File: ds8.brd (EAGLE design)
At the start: 127 x 66 mm, 114 parts, among them IC1 TM4C1230C3PM, IC2 TPS77333, IC3 DAC7512, J1 9VDC POSITIVE CENTER, Q1 BC850, Q2 BC850, Q3 BC850, U1 LM13700M, U100 VREG-7805-DPAK2, U2 LM324, U3 LM324, U4 LM741D, X1 MIDI IN, X2 MIDI OUT

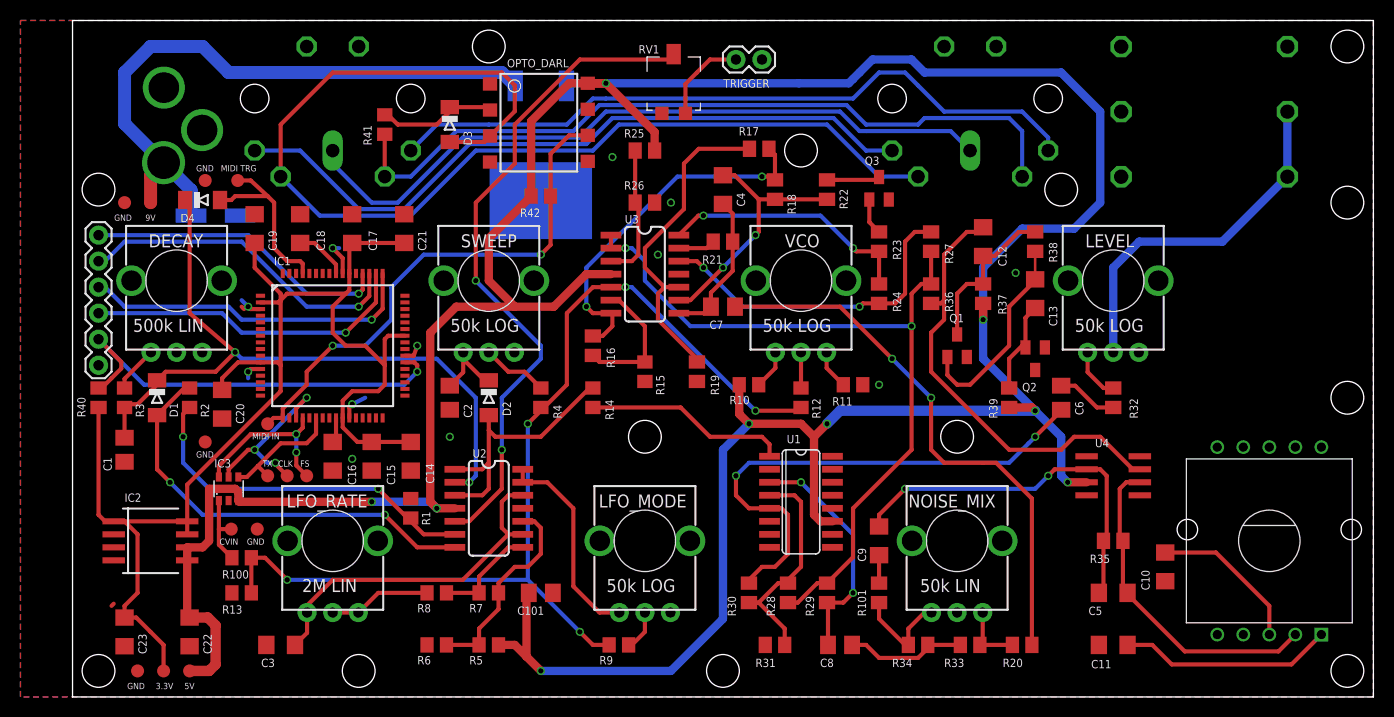
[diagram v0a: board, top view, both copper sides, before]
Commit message: Prototype v1
Version that has been produced via Seeed Studio.
Added todolist to readme.md.

Signed-off-by: Kamel Makhloufi <melka@blaste.net>
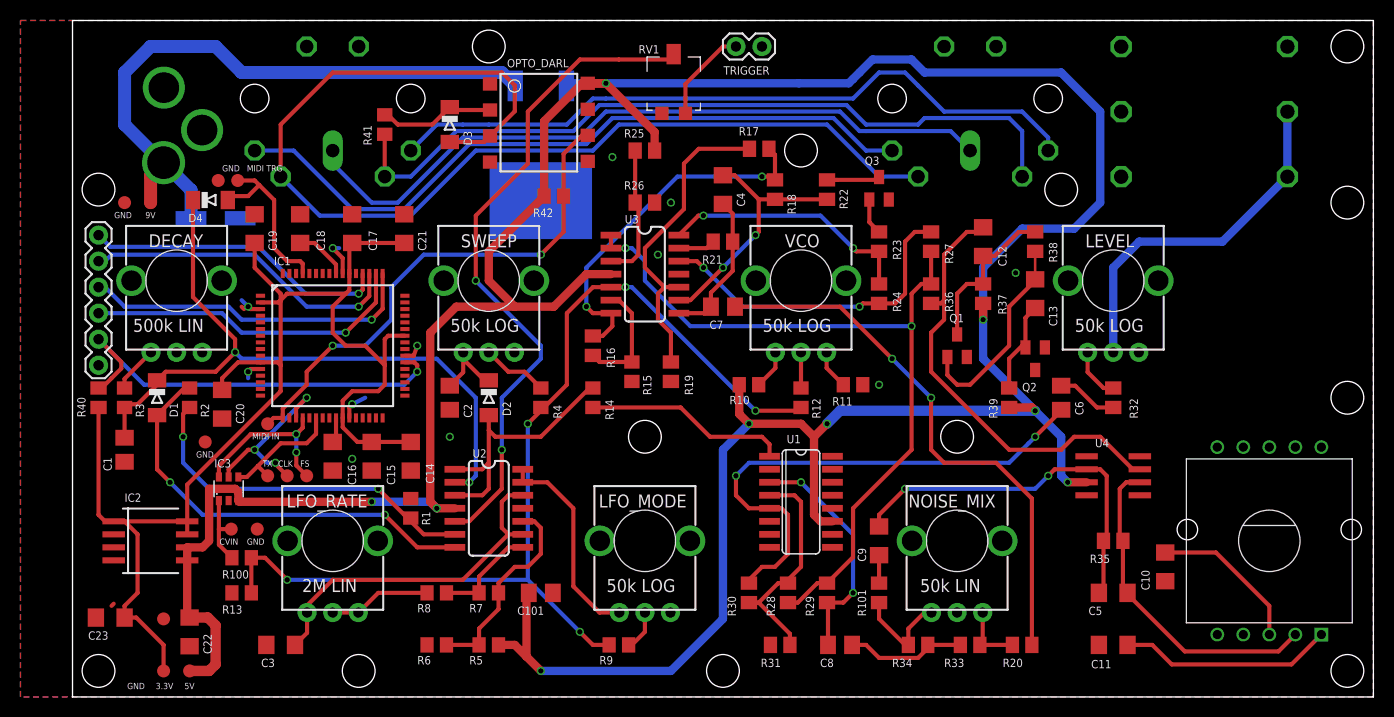
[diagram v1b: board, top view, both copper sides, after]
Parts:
- moved TP5 5.68 mm to (8.89, 7.62)
- moved R19 2.54 mm to (58.4, 31.8)
- moved C23 1.98 mm to (3.68, 7.75), turned to 0 degrees
- moved R15 1.27 mm to (54.6, 31.8)
- moved R42 1.27 mm to (47.0, 48.9)
- moved TRIGGER 1.27 mm to (67.3, 63.5)
- moved TP14 1.27 mm to (14.2, 50.4)
- moved D4 0.76 mm to (13.5, 48.5)
- moved R31 0.51 mm to (69.1, 5.08)
- moved C100 0.25 mm to (14.0, 46.7)
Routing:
- net N$7: track 13.2 -> 11.4 mm
- net TMS: track 32.5 -> 31.4 mm
- net N$10: track 32.0 -> 30.9 mm
- net VCC: track 330.2 -> 329.5 mm
- net MIDI_IN: track 51.3 -> 50.5 mm
- net N$3: track 68.6 -> 68.1 mm
- net N$34: track 8.78 -> 9.31 mm
